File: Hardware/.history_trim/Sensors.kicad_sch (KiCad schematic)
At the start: 10 parts, among them J8 Conn_01x07_Pin

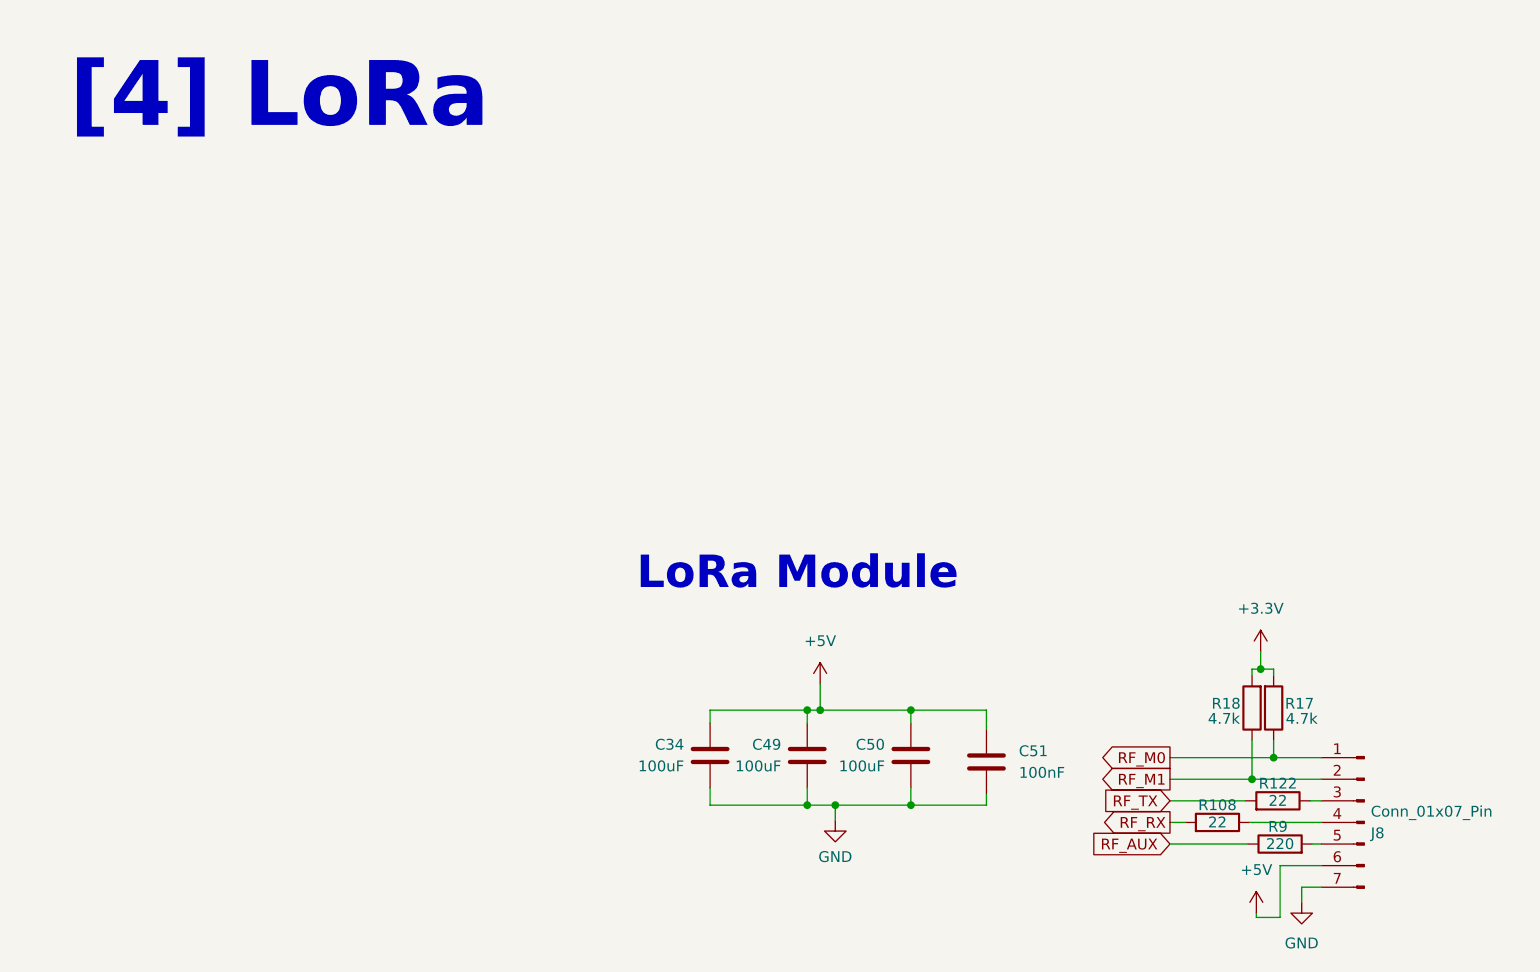
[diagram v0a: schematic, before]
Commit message: Purged heavy binaries and updated gitignore
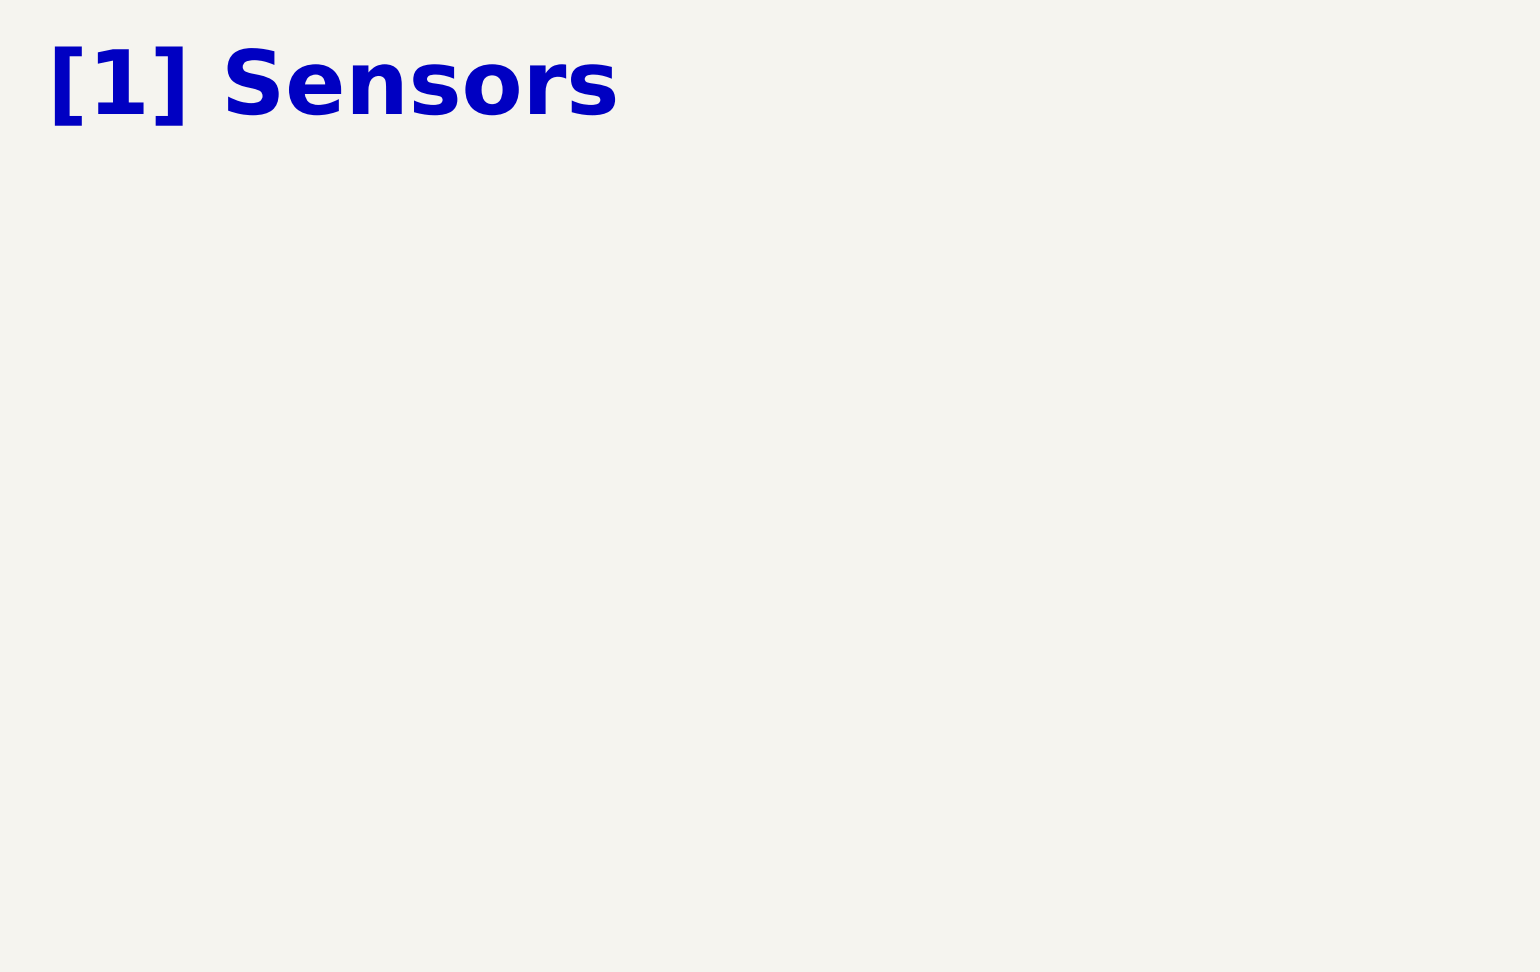
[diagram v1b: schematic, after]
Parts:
- removed C34, C49, C50: 100uF, Capacitor_Tantalum_SMD:CP_EIA-6032-20_AVX-F, symbol Device:C
- removed C51: 100nF, Capacitor_SMD:C_0603_1608Metric, symbol Device:C
- removed J8: Conn_01x07_Pin, footprints:E32-900T30D, symbol Connector:Conn_01x07_Pin
- removed R108, R122: 22, Resistor_SMD:R_0603_1608Metric, symbol Device:R
- removed R17, R18: 4.7k, Resistor_SMD:R_0603_1608Metric, symbol Device:R
- removed R9: 220, Resistor_SMD:R_0603_1608Metric, symbol Device:R
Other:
- note added: "[1] Sensors"
- note removed: "LoRa Module"
- note removed: "[4] LoRa"
- title: LoRa -> Sensors
